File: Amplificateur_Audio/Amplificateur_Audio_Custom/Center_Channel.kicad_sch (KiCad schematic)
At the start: 78 parts, among them J801 Center Tweeter+, J802 Center Tweeter-, J803 Center Woofer+, J804 Center Woofer-, U801 PCM5252RHBR, U802 TPA3244DDWR

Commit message: Assignation des composants et empreintes terminé
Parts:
- C801, C802, C805, C816, C817, C818, C819, C820, C821, C822, C823, C824, C825, C832, C833, C834, C835, C836, C841, C842, C843, C844: footprint (none) -> Capacitor_SMD:C_0603_1608Metric_Pad1.08x0.95mm_HandSolder
- C803, C804, C806, C807, C808, C809, C810, C811: footprint (none) -> Capacitor_SMD:C_0402_1005Metric_Pad0.74x0.62mm_HandSolder
- C812, C813, C814, C815, C826, C827, C828, C829, C830, C831: footprint (none) -> Capacitor_SMD:C_1206_3216Metric_Pad1.33x1.80mm_HandSolder
- C837, C838, C839, C840: footprint (none) -> Capacitor_SMD:C_1210_3225Metric_Pad1.33x2.70mm_HandSolder
- JP801, JP802, JP803, JP804: footprint (none) -> Connector_PinHeader_2.54mm:PinHeader_1x03_P2.54mm_Vertical_SMD_Pin1Left
- L801: footprint (none) -> Inductor_SMD:L_0603_1608Metric_Pad1.05x0.95mm_HandSolder
- L802, L803: footprint (none) -> NewLibrary:UA8014ALD
- R801, R809, R810, R811, R812, R813, R814, R815, R816, R817, R818, R819, R820, R821: footprint (none) -> Resistor_SMD:R_0603_1608Metric_Pad0.98x0.95mm_HandSolder
- R802, R805: value 4.99k -> 10k; footprint (none) -> Resistor_SMD:R_0402_1005Metric_Pad0.72x0.64mm_HandSolder; now not fitted
- R803: footprint (none) -> Resistor_SMD:R_0402_1005Metric_Pad0.72x0.64mm_HandSolder; now fitted
- R804: value 10k -> 4.99k; footprint (none) -> Resistor_SMD:R_0402_1005Metric_Pad0.72x0.64mm_HandSolder
- R806, R808: footprint (none) -> Resistor_SMD:R_0402_1005Metric_Pad0.72x0.64mm_HandSolder
- R807: value 10k -> 4.99k; footprint (none) -> Resistor_SMD:R_0402_1005Metric_Pad0.72x0.64mm_HandSolder; now fitted
- U801: footprint (none) -> Package_DFN_QFN:Texas_RHB0032E_VQFN-32-1EP_5x5mm_P0.5mm_EP3.45x3.45mm_ThermalVias
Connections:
- net 3.3V-2: now also C802.2, C804.2, R802.2, R805.2, R807.1, R808.2; no longer C801.2, C803.2, R803.2, R805.1, R806.1, R807.2
- net GND: now also C808.1, C825.2, R803.1, R806.1; no longer C808.2, C825.1, R802.1, R808.1
- net at R801.1, U801.14 (AVDD): now also C801.2, C803.2; no longer C802.2, C804.2
- net at U801.2 (LDOO): now also C808.2; no longer C808.1
- net at R806.2: now also R805.1, U801.22 (GPIO2/ADR2/GPO); no longer U801.1 (XSMT)
- net at U801.24 (MS/MODE2): now also R807.2; no longer R805.2
- net at U802.9 (AVDD): now also C825.1; no longer C825.2
- net at U801.23 (MODE1): now also R804.2; no longer R802.2
- new net: R808.1, U801.1 (XSMT)
- new net: R802.1, R803.2, U801.32 (MISO(GPIO1)/ADR1/FMT)

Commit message: Ajout de point de test et début du routage
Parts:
- C830, C831: footprint Capacitor_SMD:C_1206_3216Metric_Pad1.33x1.80mm_HandSolder -> Capacitor_SMD:CP_Elec_16x17.5
- J801, J802, J803, J804: footprint (none) -> NewLibrary:630661MouserReel
- U802: footprint DDV0044D_N -> NewLibrary:DDV0044D_N
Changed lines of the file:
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@@
 	)
 	(symbol
+		(lib_id "Device:C_Polarized_Small_US")
+		(at 271.145 75.565 0)
+		(unit 1)
+		(exclude_from_sim no)
+		(in_bom yes)
+		(on_board yes)
+		(dnp no)
+		(fields_autoplaced yes)
+		(property "Reference" "C830"
+			(at 273.685 73.8631 0)
+			(effects
+				(font
+					(size 1.27 1.27)
+				)
+				(justify left)
+			)
+		)
+		(property "Value" "1000uF"
+			(at 273.685 76.4031 0)
+			(effects
+				(font
+					(size 1.27 1.27)
+				)
+				(justify left)
+			)
+		)
+		(property "Footprint" "Capacitor_SMD:CP_Elec_16x17.5"
+			(at 271.145 75.565 0)
+			(effects
+				(font
+					(size 1.27 1.27)
+				)
+				(hide yes)
+			)
+		)
+		(property "Datasheet" "~"
+			(at 271.145 75.565 0)
+			(effects
+				(font
+					(size 1.27 1.27)
+				)
+				(hide yes)
+			)
+		)
+		(property "Description" "EEV-FK1H102M"
+			(at 271.145 75.565 0)
+			(effects
+				(font
+					(size 1.27 1.27)
+				)
+				(hide yes)
+			)
+		)
+		(pin "1"
+		)
+		(pin "2"
+		)
+		(instances
+			(project "Amplificateur_Audio"
+				(path "/bf9cc67f-178f-4c8c-b6a6-249a1896d599/c036bfb0-bbd6-4b06-9ac2-4fee91403ada"
+					(reference "C830")
+					(unit 1)
+				)
+			)
+		)
+	)
+	(symbol
 		(lib_id "Connector:Conn_01x01_Pin")
 		(at 389.255 180.975 180)
@@
 			)
 		)
-		(property "Footprint" ""
+		(property "Footprint" "NewLibrary:630661MouserReel"
 			(at 389.255 180.975 0)
 			(effects
@@
 	)
 	(symbol
-		(lib_id "Device:C_Polarized_Small_US")
-		(at 277.495 94.615 0)
-		(unit 1)
-		(exclude_from_sim no)
-		(in_bom yes)
-		(on_board yes)
-		(dnp no)
-		(fields_autoplaced yes)
-		(property "Reference" "C831"
-			(at 280.035 92.9131 0)
-			(effects
-				(font
-					(size 1.27 1.27)
-				)
-				(justify left)
-			)
-		)
-		(property "Value" "1000uF"
-			(at 280.035 95.4531 0)
-			(effects
-				(font
-					(size 1.27 1.27)
-				)
-				(justify left)
-			)
-		)
-		(property "Footprint" "Capacitor_SMD:C_1206_3216Metric_Pad1.33x1.80mm_HandSolder"
-			(at 277.495 94.615 0)
-			(effects
-				(font
-					(size 1.27 1.27)
-				)
-				(hide yes)
-			)
-		)
-		(property "Datasheet" "~"
-			(at 277.495 94.615 0)
-			(effects
-				(font
-					(size 1.27 1.27)
-				)
-				(hide yes)
-			)
-		)
-		(property "Description" "GRM31MR71H105KA88L"
-			(at 277.495 94.615 0)
-			(effects
-				(font
-					(size 1.27 1.27)
-				)
-				(hide yes)
-			)
-		)
-		(pin "1"
-		)
-		(pin "2"
-		)
-		(instances
-			(project "Amplificateur_Audio"
-				(path "/bf9cc67f-178f-4c8c-b6a6-249a1896d599/c036bfb0-bbd6-4b06-9ac2-4fee91403ada"
-					(reference "C831")
-					(unit 1)
-				)
-			)
-		)
-	)
-	(symbol
 		(lib_id "power:+3V3")
 		(at 58.42 153.67 0)
@@
 			)
 		)
-		(property "Footprint" ""
+		(property "Footprint" "NewLibrary:630661MouserReel"
 			(at 389.255 114.935 0)
 			(effects
@@
 			)
 		)
-		(property "Footprint" "DDV0044D_N"
+		(property "Footprint" "NewLibrary:DDV0044D_N"
 			(at 276.225 183.515 0)
 			(effects
@@
 	)
 	(symbol
-		(lib_id "Device:C_Polarized_Small_US")
-		(at 271.145 75.565 0)
-		(unit 1)
-		(exclude_from_sim no)
-		(in_bom yes)
-		(on_board yes)
-		(dnp no)
-		(fields_autoplaced yes)
-		(property "Reference" "C830"
-			(at 273.685 73.8631 0)
-			(effects
-				(font
-					(size 1.27 1.27)
-				)
-				(justify left)
-			)
-		)
-		(property "Value" "1000uF"
-			(at 273.685 76.4031 0)
-			(effects
-				(font
-					(size 1.27 1.27)
-				)
-				(justify left)
-			)
-		)
-		(property "Footprint" "Capacitor_SMD:C_1206_3216Metric_Pad1.33x1.80mm_HandSolder"
-			(at 271.145 75.565 0)
-			(effects
-				(font
-					(size 1.27 1.27)
-				)
-				(hide yes)
-			)
-		)
-		(property "Datasheet" "~"
-			(at 271.145 75.565 0)
-			(effects
-				(font
-					(size 1.27 1.27)
-				)
-				(hide yes)
-			)
-		)
-		(property "Description" "GRM31MR71H105KA88L"
-			(at 271.145 75.565 0)
-			(effects
-				(font
-					(size 1.27 1.27)
-				)
-				(hide yes)
-			)
-		)
-		(pin "1"
-		)
-		(pin "2"
-		)
-		(instances
-			(project "Amplificateur_Audio"
-				(path "/bf9cc67f-178f-4c8c-b6a6-249a1896d599/c036bfb0-bbd6-4b06-9ac2-4fee91403ada"
-					(reference "C830")
-					(unit 1)
-				)
-			)
-		)
-	)
-	(symbol
 		(lib_id "Device:R_Small")
 		(at 47.625 88.9 180)
@@
 			)
 		)
-		(property "Footprint" ""
+		(property "Footprint" "NewLibrary:630661MouserReel"
 			(at 389.255 159.385 0)
 			(effects
@@
 	)
 	(symbol
+		(lib_id "Device:C_Polarized_Small_US")
+		(at 277.495 94.615 0)
+		(unit 1)
+		(exclude_from_sim no)
+		(in_bom yes)
+		(on_board yes)
+		(dnp no)
+		(fields_autoplaced yes)
+		(property "Reference" "C831"
+			(at 280.035 92.9131 0)
+			(effects
+				(font
+					(size 1.27 1.27)
+				)
+				(justify left)
+			)
+		)
+		(property "Value" "1000uF"
+			(at 280.035 95.4531 0)
+			(effects
+				(font
+					(size 1.27 1.27)
+				)
+				(justify left)
+			)
+		)
+		(property "Footprint" "Capacitor_SMD:CP_Elec_16x17.5"
+			(at 277.495 94.615 0)
+			(effects
+				(font
+					(size 1.27 1.27)
+				)
+				(hide yes)
+			)
+		)
+		(property "Datasheet" "~"
+			(at 277.495 94.615 0)
+			(effects
+				(font
+					(size 1.27 1.27)
+				)
+				(hide yes)
+			)
+		)
+		(property "Description" "EEV-FK1H102M"
+			(at 277.495 94.615 0)
+			(effects
+				(font
+					(size 1.27 1.27)
+				)
+				(hide yes)
+			)
+		)
+		(pin "1"
+		)
+		(pin "2"
+		)
+		(instances
+			(project "Amplificateur_Audio"
+				(path "/bf9cc67f-178f-4c8c-b6a6-249a1896d599/c036bfb0-bbd6-4b06-9ac2-4fee91403ada"
+					(reference "C831")
+					(unit 1)
+				)
+			)
+		)
+	)
+	(symbol
 		(lib_id "power:Earth")
 		(at 263.525 78.105 0)
@@
 			)
 		)
-		(property "Footprint" ""
+		(property "Footprint" "NewLibrary:630661MouserReel"
 			(at 389.255 136.525 0)
 			(effects

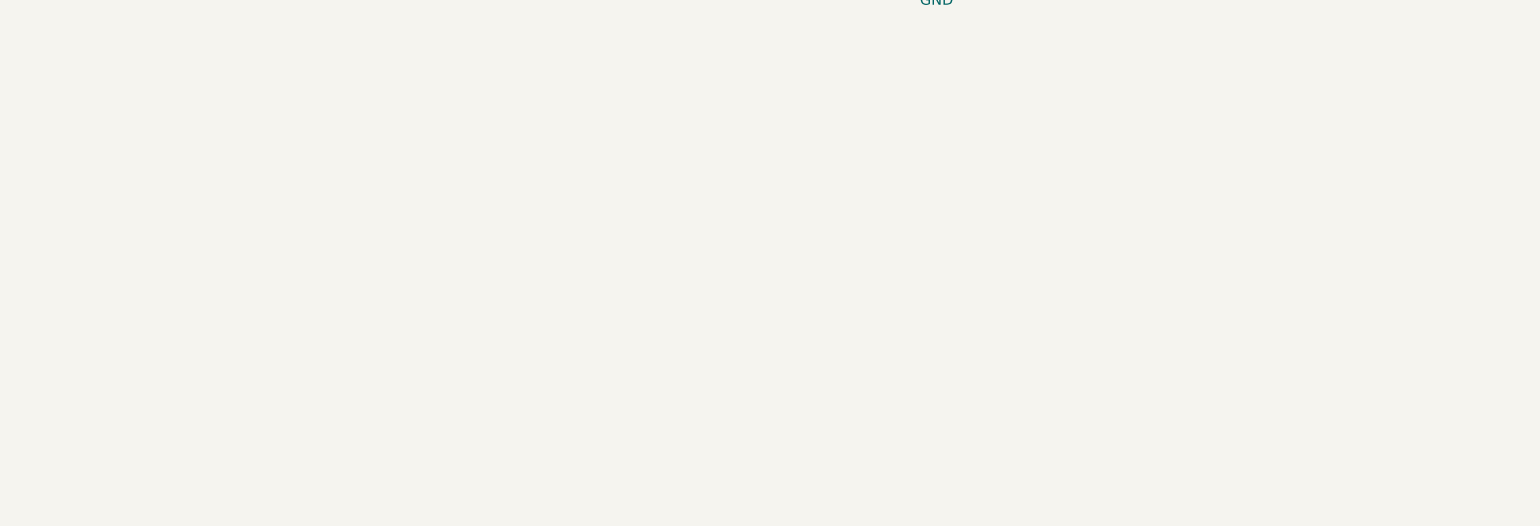
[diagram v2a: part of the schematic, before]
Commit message: Routage finale pour Surround Channel, publication d'une backup avant clonage grace au multichannel
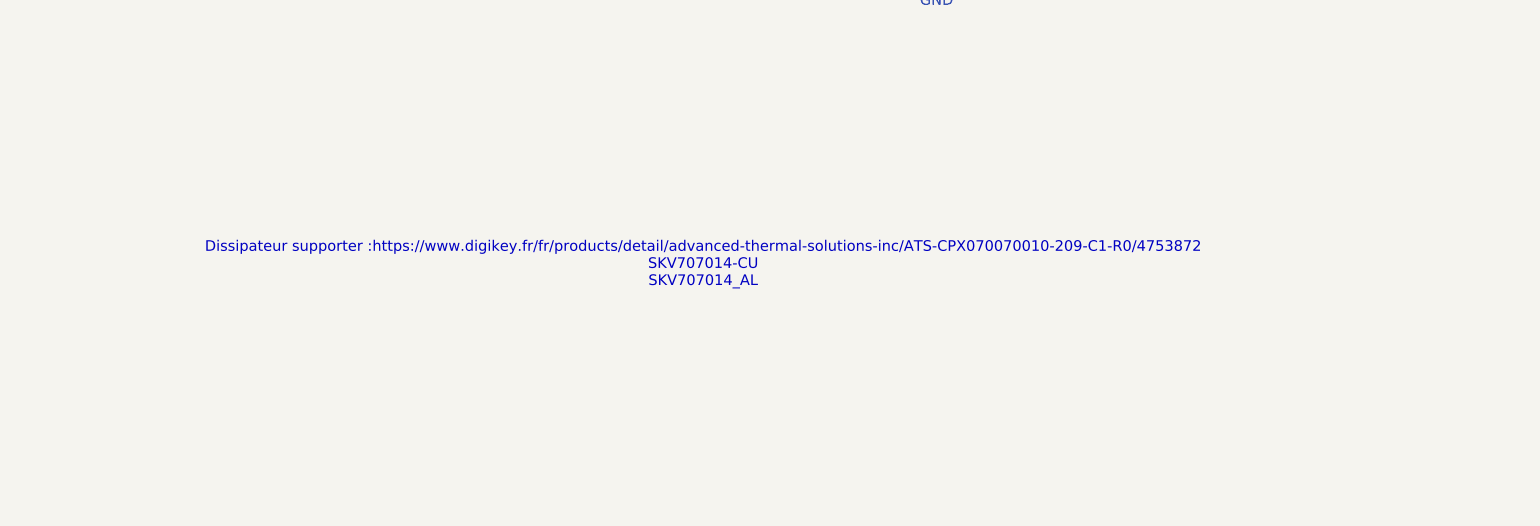
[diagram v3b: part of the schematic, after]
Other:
- note added: "Dissipateur supporter :https://www.digikey.fr/fr/products/detail/advanced-thermal-solutions-inc/ATS-CPX070070010-209-C1-R0/4753872 SKV707014-CU SKV707014_AL"
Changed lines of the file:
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@@
+		)
+	)
+	(text "Dissipateur supporter :https://www.digikey.fr/fr/products/detail/advanced-thermal-solutions-inc/ATS-CPX070070010-209-C1-R0/4753872\nSKV707014-CU\nSKV707014_AL"
+		(exclude_from_sim no)
+		(at 93.98 190.5 0)
+		(effects
+			(font
+				(size 1.27 1.27)
+			)
 		)
 	)

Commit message: Refactor : hierarchical template channels for multichannel routing
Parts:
- removed JP801, JP802, JP803, JP804: Jumper_3_Open, Connector_PinHeader_2.54mm:PinHeader_1x03_P2.54mm_Vertical_SMD_Pin1Left, symbol Jumper:Jumper_3_Open
- added C824, C827: 0.1uF, Capacitor_SMD:C_0603_1608Metric, symbol Device:C_Small
- C801, C802, C805, C816, C817, C818, C819, C820, C821, C822, C823: footprint Capacitor_SMD:C_0603_1608Metric_Pad1.08x0.95mm_HandSolder -> Capacitor_SMD:C_0603_1608Metric
- C803, C804, C806, C809, C810, C811: footprint Capacitor_SMD:C_0402_1005Metric_Pad0.74x0.62mm_HandSolder -> Capacitor_SMD:C_0402_1005Metric
- C807: renamed from C808; footprint Capacitor_SMD:C_0402_1005Metric_Pad0.74x0.62mm_HandSolder -> Capacitor_SMD:C_0402_1005Metric
- C808: renamed from C807; footprint Capacitor_SMD:C_0402_1005Metric_Pad0.74x0.62mm_HandSolder -> Capacitor_SMD:C_0402_1005Metric
- C812, C813, C814, C815: footprint Capacitor_SMD:C_1206_3216Metric_Pad1.33x1.80mm_HandSolder -> Capacitor_SMD:C_1206_3216Metric
- C825: renamed from C824; footprint Capacitor_SMD:C_0603_1608Metric_Pad1.08x0.95mm_HandSolder -> Capacitor_SMD:C_0603_1608Metric
- C826: renamed from C825; footprint Capacitor_SMD:C_0603_1608Metric_Pad1.08x0.95mm_HandSolder -> Capacitor_SMD:C_0603_1608Metric
- C828: renamed from C826; footprint Capacitor_SMD:C_1206_3216Metric_Pad1.33x1.80mm_HandSolder -> Capacitor_SMD:C_1206_3216Metric
- C829: renamed from C827; footprint Capacitor_SMD:C_1206_3216Metric_Pad1.33x1.80mm_HandSolder -> Capacitor_SMD:C_1206_3216Metric
- C830: renamed from C828; footprint Capacitor_SMD:C_1206_3216Metric_Pad1.33x1.80mm_HandSolder -> Capacitor_SMD:C_1206_3216Metric
- C831: renamed from C829; footprint Capacitor_SMD:C_1206_3216Metric_Pad1.33x1.80mm_HandSolder -> Capacitor_SMD:C_1206_3216Metric
- C832: renamed from C830; footprint Capacitor_SMD:CP_Elec_16x17.5 -> NewLibrary:CAP_EEVFK1H102M
- C833: renamed from C831; footprint Capacitor_SMD:CP_Elec_16x17.5 -> NewLibrary:CAP_EEVFK1H102M
- C834: renamed from C832; footprint Capacitor_SMD:C_0603_1608Metric_Pad1.08x0.95mm_HandSolder -> Capacitor_SMD:C_0603_1608Metric
- C835: renamed from C833; footprint Capacitor_SMD:C_0603_1608Metric_Pad1.08x0.95mm_HandSolder -> Capacitor_SMD:C_0603_1608Metric
- C836: renamed from C834; footprint Capacitor_SMD:C_0603_1608Metric_Pad1.08x0.95mm_HandSolder -> Capacitor_SMD:C_0603_1608Metric
- C837: renamed from C835; footprint Capacitor_SMD:C_0603_1608Metric_Pad1.08x0.95mm_HandSolder -> Capacitor_SMD:C_0603_1608Metric
- C838: renamed from C836; footprint Capacitor_SMD:C_0603_1608Metric_Pad1.08x0.95mm_HandSolder -> Capacitor_SMD:C_0603_1608Metric
- C839: renamed from C837; footprint Capacitor_SMD:C_1210_3225Metric_Pad1.33x2.70mm_HandSolder -> Capacitor_SMD:C_1210_3225Metric
- C840: renamed from C838; footprint Capacitor_SMD:C_1210_3225Metric_Pad1.33x2.70mm_HandSolder -> Capacitor_SMD:C_1210_3225Metric
- C841: renamed from C839; footprint Capacitor_SMD:C_1210_3225Metric_Pad1.33x2.70mm_HandSolder -> Capacitor_SMD:C_1210_3225Metric
- C842: renamed from C840; footprint Capacitor_SMD:C_1210_3225Metric_Pad1.33x2.70mm_HandSolder -> Capacitor_SMD:C_1210_3225Metric
- C843: renamed from C841; footprint Capacitor_SMD:C_0603_1608Metric_Pad1.08x0.95mm_HandSolder -> Capacitor_SMD:C_0603_1608Metric
- C844: renamed from C842; footprint Capacitor_SMD:C_0603_1608Metric_Pad1.08x0.95mm_HandSolder -> Capacitor_SMD:C_0603_1608Metric
- C845: renamed from C843; footprint Capacitor_SMD:C_0603_1608Metric_Pad1.08x0.95mm_HandSolder -> Capacitor_SMD:C_0603_1608Metric
- C846: renamed from C844; footprint Capacitor_SMD:C_0603_1608Metric_Pad1.08x0.95mm_HandSolder -> Capacitor_SMD:C_0603_1608Metric
- R801, R813, R814, R815, R816, R817: footprint Resistor_SMD:R_0603_1608Metric_Pad0.98x0.95mm_HandSolder -> Resistor_SMD:R_0603_1608Metric
- R802, R803, R804, R805, R806, R807, R808: footprint Resistor_SMD:R_0402_1005Metric_Pad0.72x0.64mm_HandSolder -> Resistor_SMD:R_0402_1005Metric
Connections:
- net DAC5L+: now also C812.1
- net DAC5L-: now also C813.1
- net DAC5R+: now also C815.1
- net DAC5R-: now also C814.1
- net GND: now also C824.1, C827.1
- net PVDD: now also C824.2, C827.2
- net DACF5L+: now reaches C812.2, R813.2
- net DACF5R+: now reaches C815.2, R816.2
- net LDOO: now reaches C807.2, U801.2 (LDOO)
- net MODE1: now reaches R804.2, U801.23 (MODE1)
- net ADR2: now reaches R805.1, R806.2, U801.22 (GPIO2/ADR2/GPO)
- net XSMT: now reaches R808.1, U801.1 (XSMT)
- net VNEG: now reaches C809.1, U801.9 (VNEG)
- net MISO: now reaches R802.1, R803.2, U801.32 (MISO(GPIO1)/ADR1/FMT)
- net DACF5L-: now reaches C813.2, R814.2
- net AVDD: now reaches C801.2, C803.2, R801.1, U801.14 (AVDD)
- net CAPP: now reaches C808.1, U801.6 (CAPP)
- net CAPM: now reaches C808.2, U801.8 (CAPM)
- net DACF5R-: now reaches C814.2, R815.2
- net MODE2: now reaches R807.2, U801.24 (MS/MODE2)
- net INPUTA5 renamed INPUTL5+
- net INPUTB5 renamed INPUTL5-
- net INPUTC5 renamed INPUTR5-
- net INPUTD5 renamed INPUTR5+
- net OUTLN5 renamed OUTL5-
- net OUTLP5 renamed OUTL5+
- net OUTRN5 renamed OUTR5-
- net OUTRP5 renamed OUTR5+
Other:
- note removed: "FROM INPUT HEADER"
- moved on the sheet: C808, C820, C821, C822, C823, C825, C826, C828, C829, C830, C831, C832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
